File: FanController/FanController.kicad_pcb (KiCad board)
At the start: 2 copper layers, 16 parts, among them J1 Conn_01x02, J2 Conn_01x02, J3 Conn_01x02, Q1 BTA16, U1 MOC3020, U2 EL817, U3 NodeMCU1.0(ESP-12E)

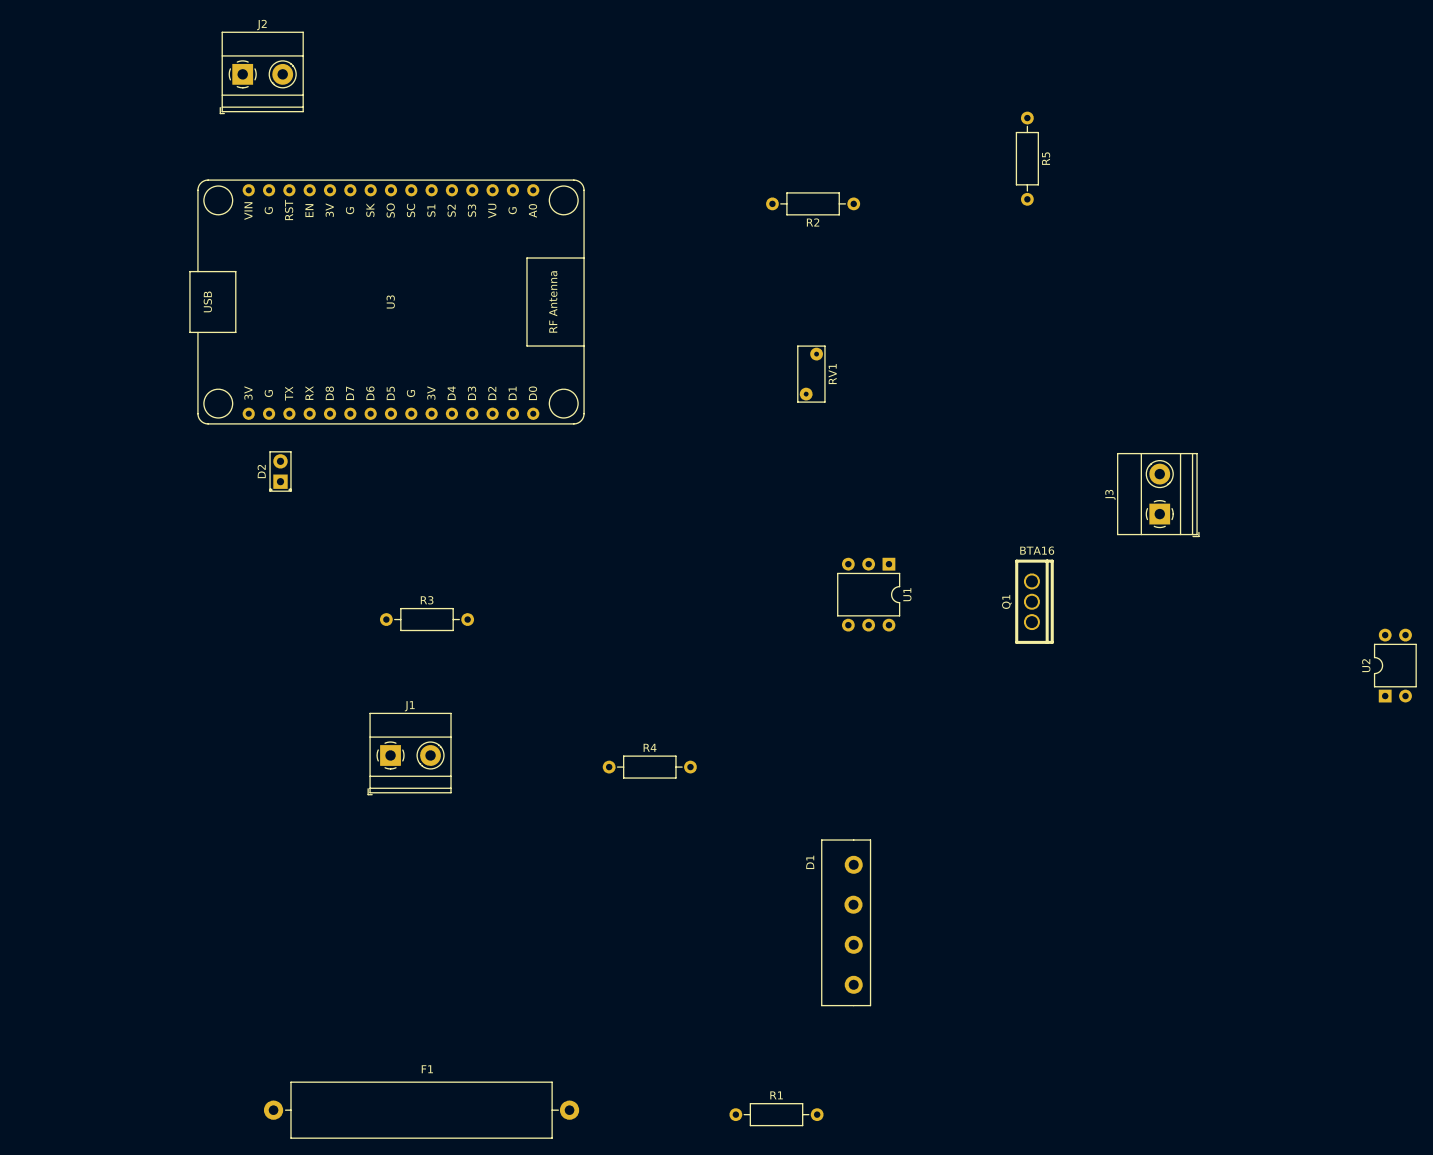
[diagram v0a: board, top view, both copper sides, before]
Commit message: placed components in a preliminary location
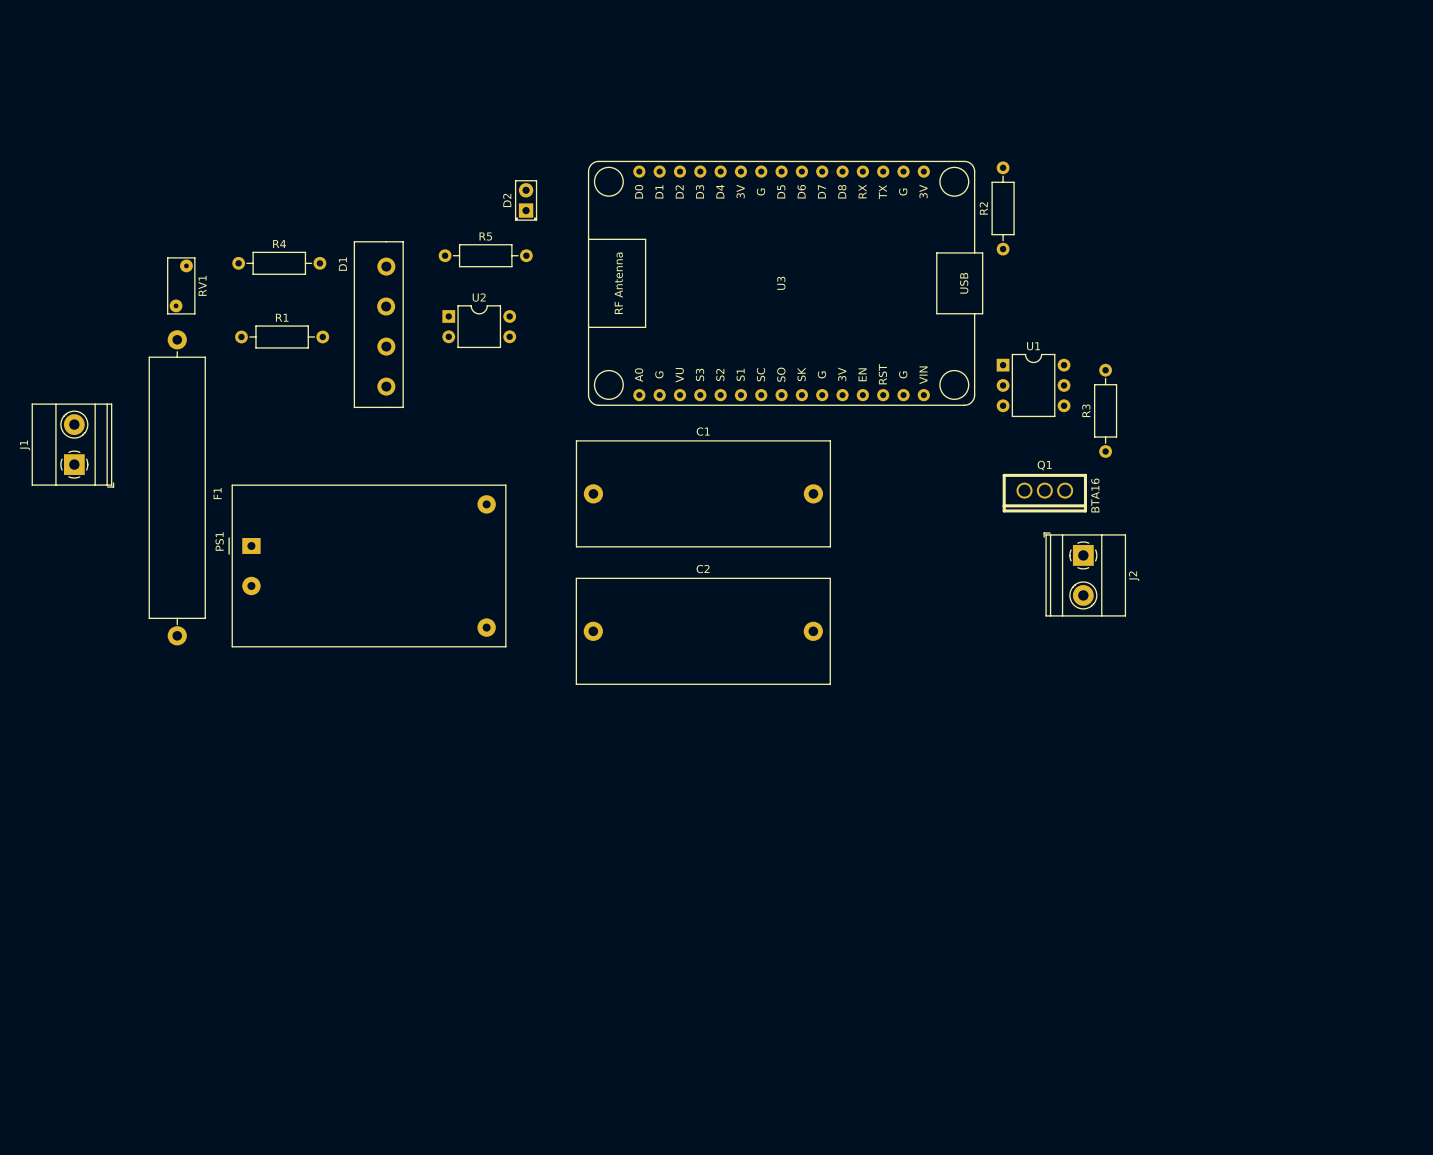
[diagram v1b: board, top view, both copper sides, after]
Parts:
- removed J3: Conn_01x02, TerminalBlock_Phoenix:TerminalBlock_Phoenix_MKDS-1,5-2_1x02_P5.00mm_Horizontal
- added C1: 10uf, Capacitor_THT:C_Rect_L31.5mm_W13.0mm_P27.50mm_MKS4, F.Cu at (106.1, 90.7)
- added C2: 22uf, Capacitor_THT:C_Rect_L31.5mm_W13.0mm_P27.50mm_MKS4, F.Cu at (106.1, 107.8)
- added PS1: HLK-PM03, Converter_ACDC:Converter_ACDC_HiLink_HLK-PMxx, F.Cu at (63.3, 97.2)
- J1: value Conn_01x02 -> AC
- J2: value Conn_01x02 -> AC Out
- moved U2 126.3 mm to (88.0, 68.5), turned to 0 degrees
- moved J2 121.1 mm to (167.3, 98.3), turned to 270 degrees
- moved R1 115.2 mm to (62.1, 71.0)
- moved D1 94.9 mm to (80.2, 62.2)
- moved R3 92.3 mm to (170.1, 85.4), turned to 90 degrees
- moved RV1 79.5 mm to (53.9, 67.2)
- moved R4 78.2 mm to (61.7, 61.8)
- moved F1 76.9 mm to (54.1, 108.4), turned to 90 degrees
- moved R5 74.8 mm to (87.5, 60.9), turned to 0 degrees
- moved J1 53.7 mm to (41.2, 87.0), turned to 90 degrees
- moved U3 48.9 mm to (129.6, 64.3), turned to 90 degrees
- moved D2 45.7 mm to (97.7, 55.2)
- moved U1 28.7 mm to (157.3, 74.6), turned to 0 degrees
- moved R2 19.5 mm to (157.3, 60.1), turned to 90 degrees
- moved Q1 14.0 mm to (162.5, 90.2), turned to 270 degrees
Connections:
- J1 pad 1: 220AC -> Net-(F1-Pad1)
- J2 pad 1: VDD -> Fase_out
- J2 pad 2: GND_VDD -> Neutro
- R1 pad 1: Net-(F1-Pad1) -> 220AC
- U3 pad 14: GND_VDD -> +3V3
- U3 pad 15: VDD -> GND
